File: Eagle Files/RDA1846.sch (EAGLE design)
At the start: 42 parts, among them X1 SMA-142-0701-871/876, X2 SMA-142-0701-871/876, X3 SMA-142-0701-871/876

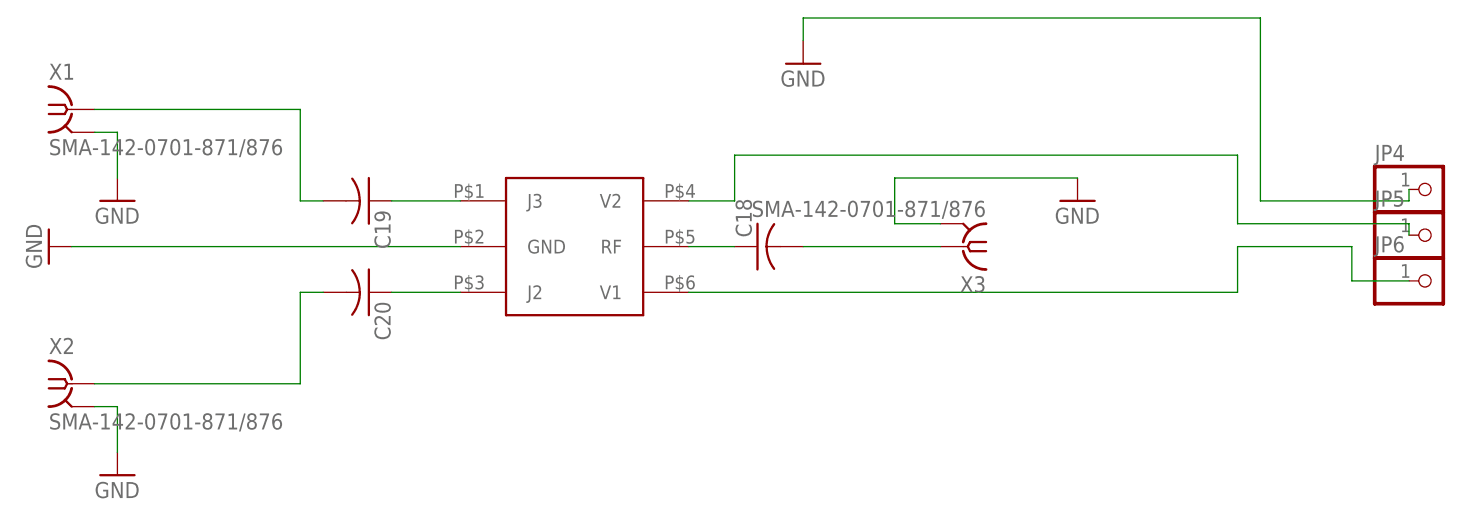
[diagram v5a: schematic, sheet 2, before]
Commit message: Placed all the names and values. QA remaining
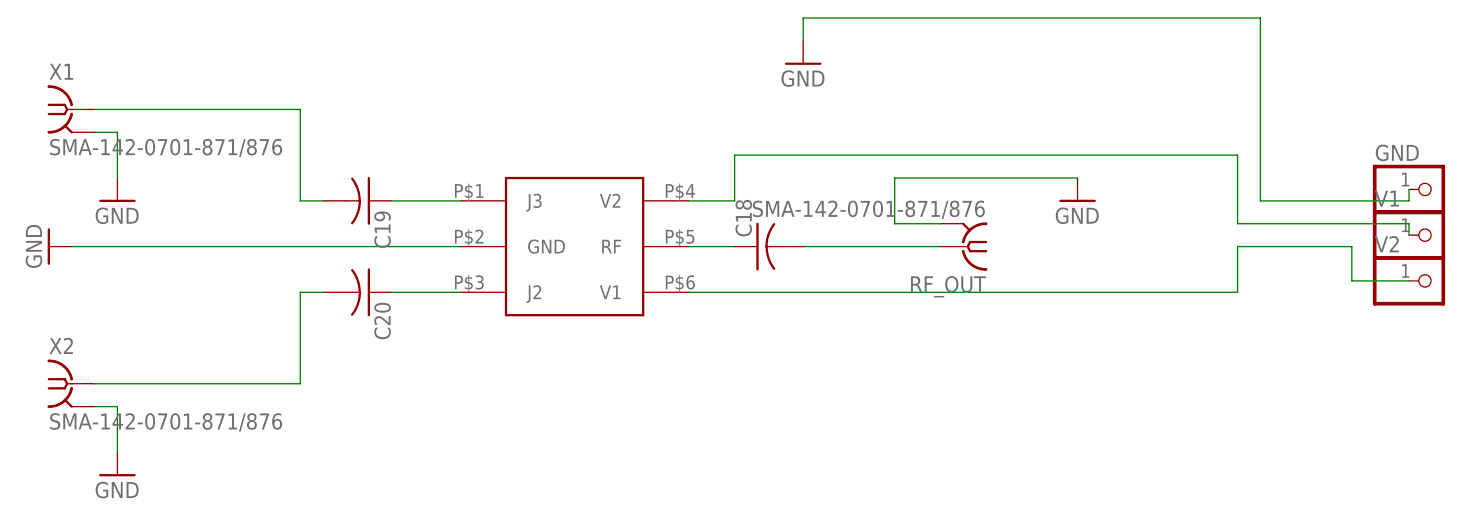
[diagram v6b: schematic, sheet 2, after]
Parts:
- renumbered JP2 to SCLK, JP3 to MODE_SENB_GND, JP4 to GND, JP5 to V1, JP6 to V2, JP7 to SDIO, X3 to RF_OUT
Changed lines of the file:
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@@
 <part name="X1" library="con-coax" deviceset="SMA-" device="142-0701-871/876"/>
 <part name="X2" library="con-coax" deviceset="SMA-" device="142-0701-871/876"/>
-<part name="X3" library="con-coax" deviceset="SMA-" device="142-0701-871/876"/>
+<part name="RF_OUT" library="con-coax" deviceset="SMA-" device="142-0701-871/876"/>
 <part name="GND28" library="supply1" deviceset="GND" device=""/>
 <part name="GND29" library="supply1" deviceset="GND" device=""/>
@@
 <part name="GND31" library="supply1" deviceset="GND" device=""/>
 <part name="GND32" library="supply1" deviceset="GND" device=""/>
-<part name="JP3" library="pinhead" deviceset="PINHD-1X3" device=""/>
+<part name="MODE_SENB_GND" library="pinhead" deviceset="PINHD-1X3" device=""/>
 <part name="JP1" library="pinhead" deviceset="PINHD-1X2" device=""/>
-<part name="JP4" library="pinhead" deviceset="PINHD-1X1" device=""/>
-<part name="JP5" library="pinhead" deviceset="PINHD-1X1" device=""/>
-<part name="JP6" library="pinhead" deviceset="PINHD-1X1" device=""/>
-<part name="JP2" library="adafruit" deviceset="PINHD-1X1" device=""/>
-<part name="JP7" library="adafruit" deviceset="PINHD-1X1" device=""/>
+<part name="GND" library="pinhead" deviceset="PINHD-1X1" device=""/>
+<part name="V1" library="pinhead" deviceset="PINHD-1X1" device=""/>
+<part name="V2" library="pinhead" deviceset="PINHD-1X1" device=""/>
+<part name="SCLK" library="adafruit" deviceset="PINHD-1X1" device=""/>
+<part name="SDIO" library="adafruit" deviceset="PINHD-1X1" device=""/>
 </parts>
 <sheets>
@@
 <instance part="GND26" gate="1" x="62.23" y="113.03"/>
 <instance part="VDD10" gate="G$1" x="62.23" y="128.27" rot="MR0"/>
-<instance part="JP3" gate="A" x="-132.08" y="62.23" rot="R180"/>
+<instance part="MODE_SENB_GND" gate="A" x="-132.08" y="62.23" rot="R180"/>
 <instance part="JP1" gate="G$1" x="68.58" y="97.79" rot="R180"/>
-<instance part="JP2" gate="G$1" x="-137.16" y="81.28" rot="R180"/>
-<instance part="JP7" gate="G$1" x="-137.16" y="73.66" rot="R180"/>
+<instance part="SCLK" gate="G$1" x="-137.16" y="81.28" rot="R180"/>
+<instance part="SDIO" gate="G$1" x="-137.16" y="73.66" rot="R180"/>
 </instances>
 <busses>
@@
 <wire x1="-119.38" y1="62.23" x2="-124.46" y2="62.23" width="0.1524" layer="91"/>
 <wire x1="-124.46" y1="62.23" x2="-124.46" y2="59.69" width="0.1524" layer="91"/>
-<pinref part="JP3" gate="A" pin="1"/>
+<pinref part="MODE_SENB_GND" gate="A" pin="1"/>
 <wire x1="-124.46" y1="59.69" x2="-129.54" y2="59.69" width="0.1524" layer="91"/>
 </segment>
@@
 <wire x1="-129.54" y1="78.74" x2="-121.92" y2="78.74" width="0.1524" layer="91"/>
 <wire x1="-121.92" y1="78.74" x2="-121.92" y2="72.39" width="0.1524" layer="91"/>
-<pinref part="JP2" gate="G$1" pin="1"/>
+<pinref part="SCLK" gate="G$1" pin="1"/>
 <wire x1="-134.62" y1="81.28" x2="-129.54" y2="81.28" width="0.1524" layer="91"/>
 <wire x1="-129.54" y1="81.28" x2="-129.54" y2="78.74" width="0.1524" layer="91"/>
@@
 <wire x1="-134.62" y1="76.2" x2="-123.952" y2="76.2" width="0.1524" layer="91"/>
 <wire x1="-123.952" y1="76.2" x2="-123.952" y2="69.85" width="0.1524" layer="91"/>
-<pinref part="JP7" gate="G$1" pin="1"/>
+<pinref part="SDIO" gate="G$1" pin="1"/>
 <wire x1="-134.62" y1="76.2" x2="-134.62" y2="73.66" width="0.1524" layer="91"/>
 </segment>
@@
 <wire x1="-34.29" y1="35.56" x2="-17.78" y2="35.56" width="0.1524" layer="91"/>
 <wire x1="-128.27" y1="67.31" x2="-128.27" y2="64.77" width="0.1524" layer="91"/>
-<pinref part="JP3" gate="A" pin="3"/>
+<pinref part="MODE_SENB_GND" gate="A" pin="3"/>
 <wire x1="-128.27" y1="64.77" x2="-129.54" y2="64.77" width="0.1524" layer="91"/>
 </segment>
@@
 <wire x1="-116.84" y1="64.77" x2="-127" y2="64.77" width="0.1524" layer="91"/>
 <wire x1="-127" y1="64.77" x2="-127" y2="62.23" width="0.1524" layer="91"/>
-<pinref part="JP3" gate="A" pin="2"/>
+<pinref part="MODE_SENB_GND" gate="A" pin="2"/>
 <wire x1="-127" y1="62.23" x2="-129.54" y2="62.23" width="0.1524" layer="91"/>
 </segment>
@@
 <instance part="X1" gate="G1" x="7.62" y="73.66"/>
 <instance part="X2" gate="G1" x="7.62" y="43.18"/>
-<instance part="X3" gate="G1" x="106.68" y="58.42" rot="R180"/>
+<instance part="RF_OUT" gate="G1" x="106.68" y="58.42" rot="R180"/>
 <instance part="GND28" gate="1" x="12.7" y="63.5"/>
 <instance part="GND29" gate="1" x="12.7" y="33.02"/>
@@
 <instance part="GND31" gate="1" x="119.38" y="63.5"/>
 <instance part="GND32" gate="1" x="88.9" y="78.74"/>
-<instance part="JP4" gate="G$1" x="158.75" y="64.77"/>
-<instance part="JP5" gate="G$1" x="158.75" y="59.69"/>
-<instance part="JP6" gate="G$1" x="158.75" y="54.61"/>
+<instance part="GND" gate="G$1" x="158.75" y="64.77"/>
+<instance part="V1" gate="G$1" x="158.75" y="59.69"/>
+<instance part="V2" gate="G$1" x="158.75" y="54.61"/>
 </instances>
 <busses>
@@
 <wire x1="88.9" y1="83.82" x2="139.7" y2="83.82" width="0.1524" layer="91"/>
 <wire x1="139.7" y1="83.82" x2="139.7" y2="63.5" width="0.1524" layer="91"/>
-<pinref part="JP4" gate="G$1" pin="1"/>
+<pinref part="GND" gate="G$1" pin="1"/>
 <wire x1="139.7" y1="63.5" x2="156.21" y2="63.5" width="0.1524" layer="91"/>
 <wire x1="156.21" y1="63.5" x2="156.21" y2="64.77" width="0.1524" layer="91"/>
 </segment>
 <segment>
-<pinref part="X3" gate="G1" pin="2"/>
+<pinref part="RF_OUT" gate="G1" pin="2"/>
 <wire x1="104.14" y1="60.96" x2="99.06" y2="60.96" width="0.1524" layer="91"/>
 <wire x1="99.06" y1="60.96" x2="99.06" y2="66.04" width="0.1524" layer="91"/>
@@
 <segment>
 <pinref part="C18" gate="G$1" pin="2"/>
-<pinref part="X3" gate="G1" pin="1"/>
+<pinref part="RF_OUT" gate="G1" pin="1"/>
 <wire x1="88.9" y1="58.42" x2="104.14" y2="58.42" width="0.1524" layer="91"/>
 </segment>
@@
 <wire x1="137.16" y1="68.58" x2="137.16" y2="60.96" width="0.1524" layer="91"/>
 <wire x1="137.16" y1="60.96" x2="156.21" y2="60.96" width="0.1524" layer="91"/>
-<pinref part="JP5" gate="G$1" pin="1"/>
+<pinref part="V1" gate="G$1" pin="1"/>
 <wire x1="156.21" y1="60.96" x2="156.21" y2="59.69" width="0.1524" layer="91"/>
 </segment>
@@
 <wire x1="137.16" y1="58.42" x2="149.86" y2="58.42" width="0.1524" layer="91"/>
 <wire x1="149.86" y1="58.42" x2="149.86" y2="54.61" width="0.1524" layer="91"/>
-<pinref part="JP6" gate="G$1" pin="1"/>
+<pinref part="V2" gate="G$1" pin="1"/>
 <wire x1="149.86" y1="54.61" x2="156.21" y2="54.61" width="0.1524" layer="91"/>
 </segment>
